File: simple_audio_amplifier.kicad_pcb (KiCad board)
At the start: 2 copper layers, 80 x 50 mm, 38 parts, among them J1 TB006-508-02BE, J2 PJ-322, J3 TB006-508-02BE, U1 L7805CV, U2 LM386N-1

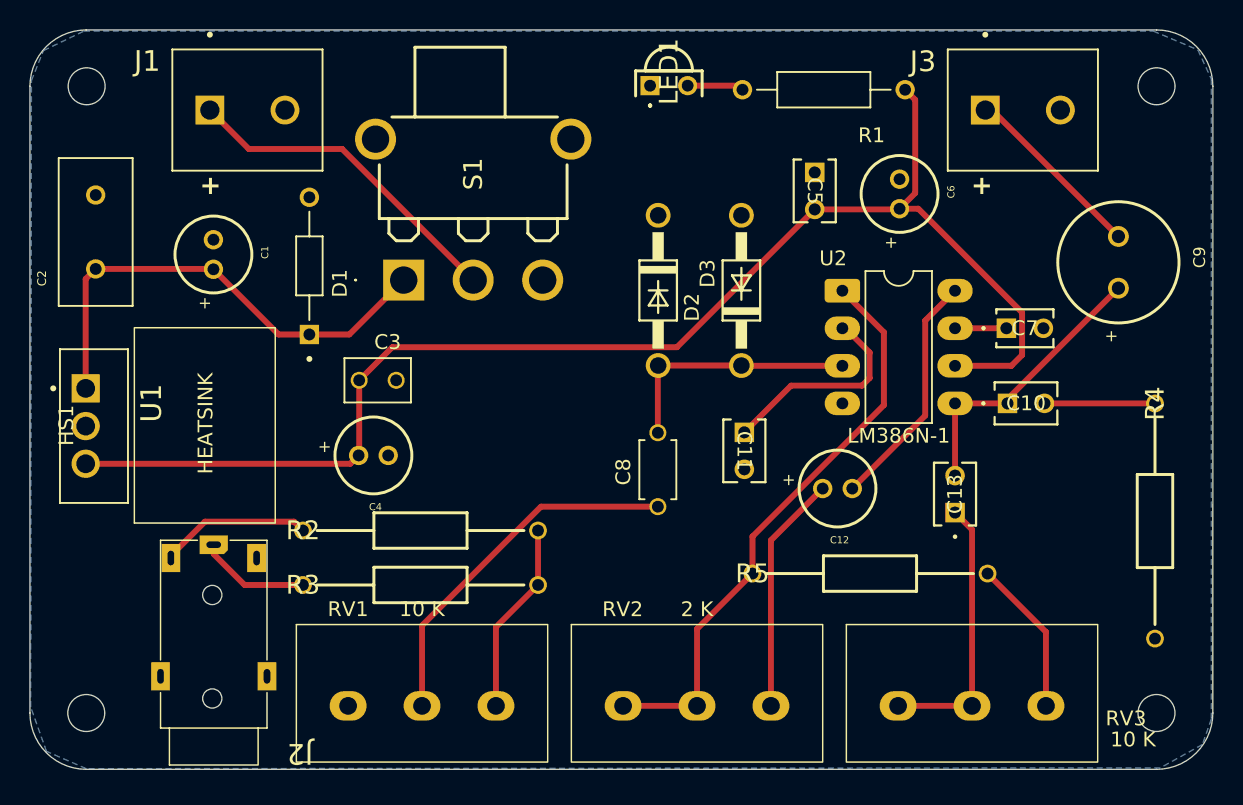
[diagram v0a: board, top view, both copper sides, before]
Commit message: Fix of silkscreen errors + 3D models
Fix: silkscreen rules are now respected.
Feat: added 3D models for 3D rendering
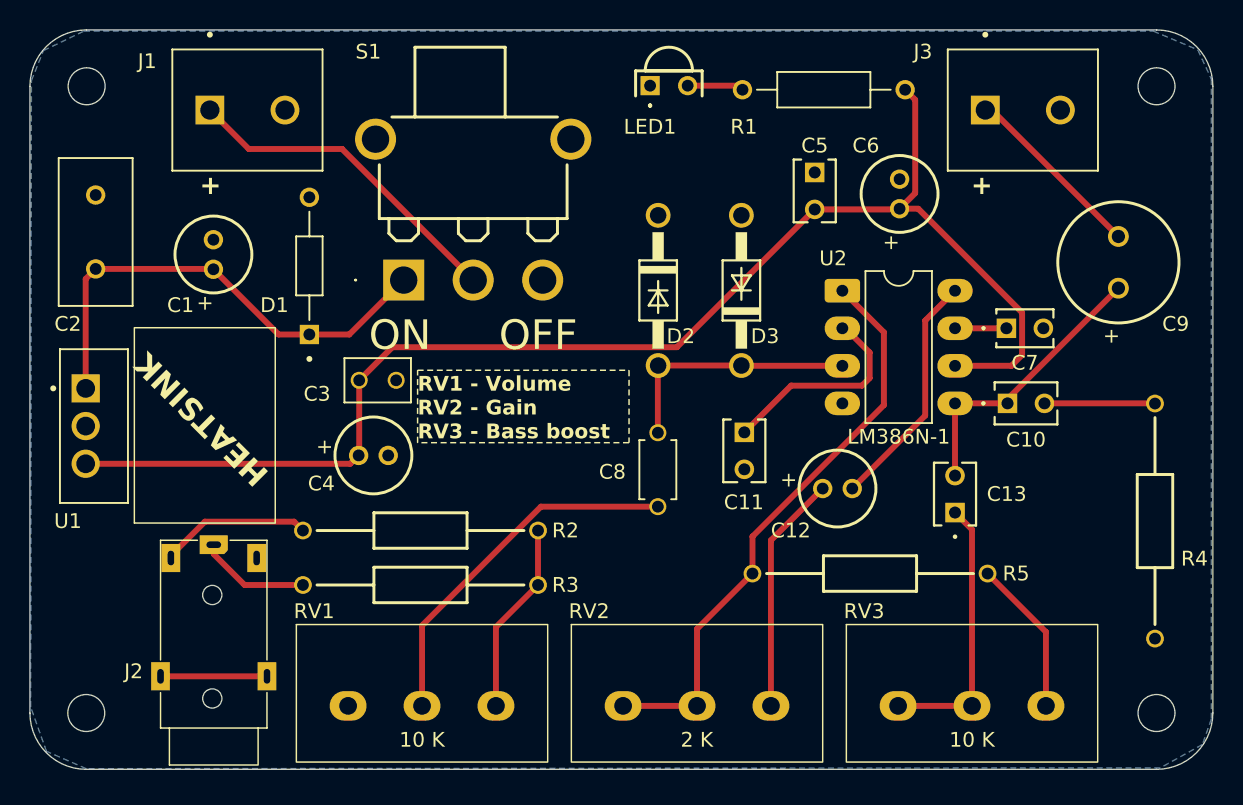
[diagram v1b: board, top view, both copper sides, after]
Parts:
- moved REF** 14.1 mm to (124.1, 96.1)
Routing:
- net unconnected-(J2-Pad3)_1: track 0.00 -> 7.20 mm
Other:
- board text added: "-"
- board text added: "Input (8-30V)"
- board text added: "OFF"
- board text added: "ON"
- board text added: "RV1 - Volume RV2 - Gain RV3 - Bass boost"
- board text removed: "Input (4-12V)"
